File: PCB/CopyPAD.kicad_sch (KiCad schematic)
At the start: 34 parts, among them J1 Conn_01x04_MountingPin, SW1 SW_Push_45deg, SW11 RotaryEncoder_Switch, SW2 SW_Push_45deg, SW3 SW_Push_45deg, SW4 SW_Push_45deg, SW5 SW_Push_45deg, SW6 SW_Push_45deg, SW7 SW_Push_45deg, SW8 SW_Push_45deg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

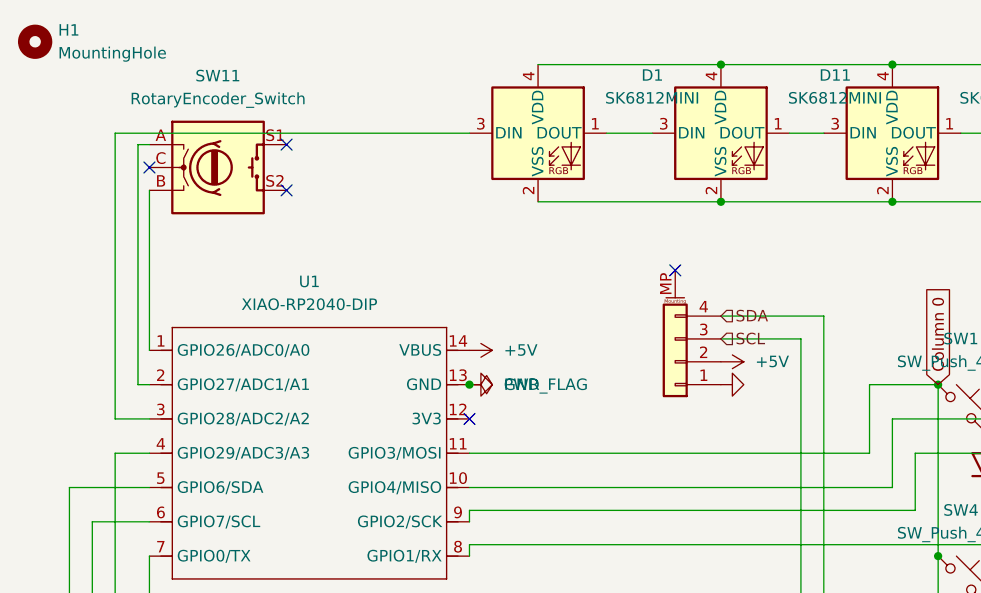
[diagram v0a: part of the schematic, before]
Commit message: fixed PCB voltadge error
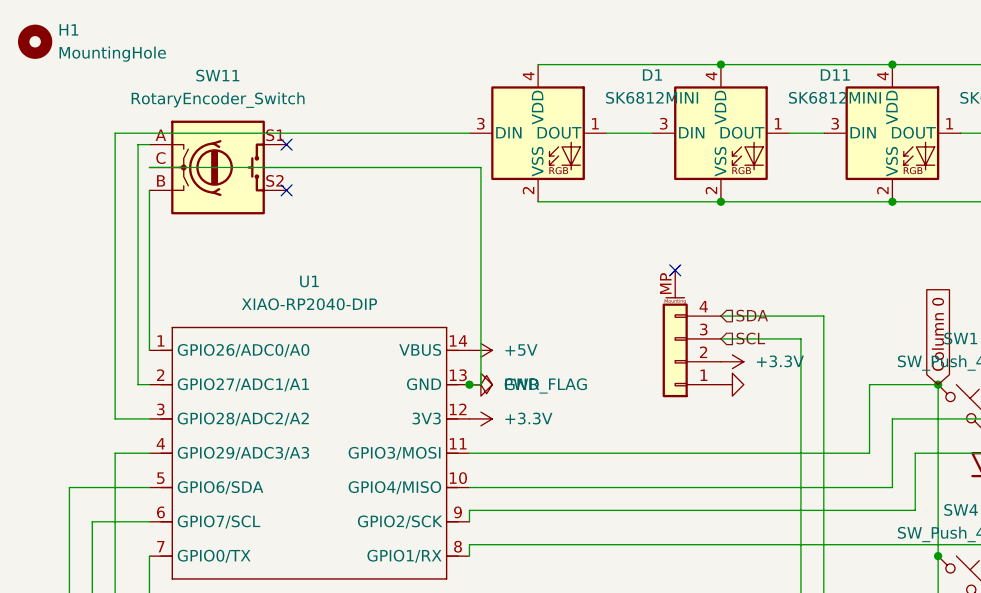
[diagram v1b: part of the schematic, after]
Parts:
- D1: footprint LED_SMD:LED_SK6812MINI_PLCC4_3.5x3.5mm_P1.75mm -> LED:BAcklight
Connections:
- net +5V: no longer J1.2 (Pin_2)
- net GND: now also SW11.C
- net +3.3V: now reaches U1.12 (3V3)
- net +3.3V: now also J1.2 (Pin_2)
- no-connect marks 6 -> 4
